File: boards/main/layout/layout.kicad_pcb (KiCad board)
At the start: 4 copper layers, 100 x 80 mm, 113 parts, among them J1 PPPC201LFBN-RC, J10 61300811121, J11 61300811121, J12 SJ1-3523N, J13 61300311121, J14 61300311121, J15 61300811121, J16 61300811121, J17 61300811121, J18 61300811121, J19 USB4085-GF-A, J2 PPPC201LFBN-RC, J3 61301021121, J4 connector, J5 61300211121, J6 61300211121, J7 SJ1-3523N, J8 61300811121, J9 61300811121, U1 ES8388, U10 NE5532DR, U2 ES8388, U3 LP2985-33DBVR, U4 MCP73831-2-OTI/OT, U5 HT8988A, U6 AP2114H-3.3TRG1, U7 CD4052BM96, U8 CD4052BM96, U9 NE5532DR

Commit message: layout
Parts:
- added C54: GRM188Z71A106KA73D, C_0603_1608Metric, F.Cu at (84.0, 30.0)
- added C55: GCM155R71H104KE02D, C_0402_1005Metric, F.Cu at (80.0, 46.0)
- added C56: GRM188Z71A106KA73D, C_0603_1608Metric, F.Cu at (84.0, 42.0)
- added C57: GCM155R71H104KE02D, C_0402_1005Metric, F.Cu at (86.0, 54.0)
- added C58: GRM188Z71A106KA73D, C_0603_1608Metric, F.Cu at (90.0, 80.0)
- added C59: GCM155R71H104KE02D, C_0402_1005Metric, F.Cu at (88.0, 70.0)
- added C60: GRM188Z71A106KA73D, C_0603_1608Metric, F.Cu at (82.0, 60.0)
- added C61: GCM155R71H104KE02D, C_0402_1005Metric, F.Cu at (94.0, 70.0)
- added R25: ERJ-2RKF1002X, R_0402_1005Metric, F.Cu at (75.4, 14.0)
- added R26: ERJ-2RKF1003X, R_0402_1005Metric, F.Cu at (68.5, 53.5)
- added R27: ERJ-2RKF1003X, R_0402_1005Metric, F.Cu at (81.0, 40.0)
- added U11: NE5532DR, SOIC-8_3.9x4.9mm_P1.27mm, F.Cu at (90.0, 64.4)
- C10: value GRM21BZ71A226ME15K -> GCM155R71H104KE02D; footprint C_0805_2012Metric -> C_0402_1005Metric
- C11: value GRM21BZ71E106KE15K -> GRM1555CYA103GE01D; footprint C_0805_2012Metric -> C_0402_1005Metric
- C14: value GRM21BZ71E106KE15K -> GRM21BZ71A226ME15K
- C15, C18: value GCM188R71E105KA64D -> GRM21BZ71E106KE15K; footprint C_0603_1608Metric -> C_0805_2012Metric
- C16, C17, C19, C20, C5: value capacitor -> GRM21BZ71E106KE15K
- C21, C22, C6: value GCM155R71H104KE02D -> GRM21BZ71E106KE15K; footprint C_0402_1005Metric -> C_0805_2012Metric
- C24, C26, C29: value GCM155R71H104KE02D -> capacitor; footprint C_0402_1005Metric -> C_0805_2012Metric
- C25, C9: value GRM21BZ71E106KE15K -> capacitor
- C27: value GRM21BZ71E106KE15K -> GCM155R71H104KE02D; footprint C_0805_2012Metric -> C_0402_1005Metric
- C28, C30: value GRM188Z71A106KA73D -> GCM155R71H104KE02D; footprint C_0603_1608Metric -> C_0402_1005Metric
- C7: value GRM1555CYA103GE01D -> GRM21BZ71E106KE15K; footprint C_0402_1005Metric -> C_0805_2012Metric
- R10, R9: value ERJ-2RKF1001X -> ERJ-2RKF1201X
- R11: value ERJ-2RKF4701X -> ERJ-2RKF1001X
- R14: value ERJ-2RKF1002X -> ERJ-2RKF4701X
- R15, R16: value ERJ-2RKF1002X -> ERJ-2RKF1001X
- R23, R24: value ERJ-2RKF1003X -> ERJ-2RKF1002X
- R3: value ERJ-2RKF1002X -> ERJ-3EKF4701V; footprint R_0402_1005Metric -> R_0603_1608Metric
- R4: value ERJ-2RKF5101X -> ERJ-3EKF4701V; footprint R_0402_1005Metric -> R_0603_1608Metric
- R5: value ERJ-2RKF5101X -> ERJ-2RKF1002X
- R6: value ERJ-2RKF1201X -> ERJ-2RKF1002X
- R7: value ERJ-2RKF1201X -> ERJ-2RKF5101X
- R8: value ERJ-2RKF1001X -> ERJ-2RKF5101X
- U3: value LP2985-33DBVR -> ES8388; footprint SOT-23-5 -> QFN-28-1EP_4x4mm_P0.4mm_EP2.4x2.4mm
- U4: value MCP73831-2-OTI/OT -> ES8388; footprint SOT-23-5 -> QFN-28-1EP_4x4mm_P0.4mm_EP2.4x2.4mm
- U5: value HT8988A -> LP2985-33DBVR; footprint QFN-28-1EP_4x4mm_P0.4mm_EP2.4x2.4mm -> SOT-23-5
- U6: value AP2114H-3.3TRG1 -> MCP73831-2-OTI/OT; footprint SOT-223-3_TabPin2 -> SOT-23-5
- U7: value CD4052BM96 -> AP2114H-3.3TRG1; footprint SOIC-16_3.9x9.9mm_P1.27mm -> SOT-223-3_TabPin2
- U9: value NE5532DR -> CD4052BM96; footprint SOIC-8_3.9x4.9mm_P1.27mm -> SOIC-16_3.9x9.9mm_P1.27mm
- moved R18 62.8 mm to (98.0, 26.0)
- moved R7 59.6 mm to (34.0, 45.5)
- moved R4 56.3 mm to (80.0, 78.0)
- moved U4 52.7 mm to (90.7, 47.9)
- moved C3 52.0 mm to (82.0, 80.0)
- moved C41 50.8 mm to (96.0, 26.0)
- moved C7 49.9 mm to (90.0, 82.0)
- moved U3 49.7 mm to (90.4, 42.0)
- moved R14 48.5 mm to (48.5, 47.5)
- moved C49 45.7 mm to (44.0, 47.5)
- moved C6 44.5 mm to (84.0, 28.0)
- moved C36 44.3 mm to (86.0, 58.0)
- moved R5 44.1 mm to (82.0, 38.0)
- moved C37 44.0 mm to (90.0, 70.0)
- moved U7 43.3 mm to (58.0, 53.0)
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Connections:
- net NC_DSDIN_A renamed NC_DSDIN_1
- net NC_DSDIN_B renamed NC_DSDIN_2
- net NC_LOUT1_A renamed NC_LOUT1_1
- net NC_LOUT1_B renamed NC_LOUT1_2
- net NC_LOUT2_A renamed NC_LOUT2_1
- net NC_LOUT2_B renamed NC_LOUT2_2
- net NC_MONO_A renamed NC_MONO_1
- net NC_MONO_B renamed NC_MONO_2
- net NC_ROUT1_A renamed NC_ROUT1_1
- net NC_ROUT1_B renamed NC_ROUT1_2
- net NC_ROUT2_A renamed NC_ROUT2_1
- net NC_ROUT2_B renamed NC_ROUT2_2
- C10 pad 1: DVDD -> VBAT
- C11 pad 1: DVREF_A1 -> LP2985_BYP
- C12 pad 1: DVREF_A2 -> DAC_OUTL
- C12 pad 2: AGND -> DAC_L_AC
- C13 pad 1: DVRP_A1 -> DAC_OUTR
- C13 pad 2: AGND -> DAC_R_AC
- C14 pad 1: DVRP_A2 -> DVDD
- C14 pad 2: AGND -> DGND
- C15 pad 1: HPCOM -> DVREF_A1
- C16 pad 1: HP_OUTL -> DVREF_A2
- C16 pad 2: HP_AC_L -> AGND
- C17 pad 1: HP_OUTR -> DVREF_A3
- C17 pad 2: HP_AC_R -> AGND
- C18 pad 1: LCOM -> DVREF_A4
- C19 pad 1: MUX1_X_FILT -> DVRP_A1
- C19 pad 2: OUT_L_AC -> AGND
- C20 pad 1: MUX1_Y_FILT -> DVRP_A2
- C20 pad 2: OUT_R_AC -> AGND
- C21 pad 1: MUX1_X_FILT -> DVRP_A3
- C22 pad 1: MUX1_Y_FILT -> DVRP_A4
- C23 pad 1: VBUS -> HP_OUTL
- C23 pad 2: DGND -> HP_AC_L
- C24 pad 1: VBUS -> HP_OUTR
- C24 pad 2: DGND -> HP_AC_R
- C25 pad 1: VMID -> MUX1_X_FILT
- C25 pad 2: AGND -> OUT_L_AC
- C26 pad 1: VBAT_DIV -> MUX1_Y_FILT
- C26 pad 2: DGND -> OUT_R_AC
- C27 pad 1: VREF -> MUX1_X_FILT
- C28 pad 1: AVDD -> MUX1_Y_FILT
- C29 pad 1: AVDD -> VBUS
- C29 pad 2: AGND -> DGND
- C3 pad 1: VRP_A1 -> VREF_A3
- C30 pad 1: AVDD -> VBUS
- C30 pad 2: AGND -> DGND
- C31 pad 1: AVDD -> VBAT_DIV
- C31 pad 2: AGND -> DGND
- C36 pad 1: DVDD -> AVDD
- C36 pad 2: DGND -> AGND
- C37 pad 1: DVDD -> AVDD
- C37 pad 2: DGND -> AGND
- C38 pad 1: DVDD -> AVDD
- C38 pad 2: DGND -> AGND
- C39 pad 1: DVDD -> AVDD
- C39 pad 2: DGND -> AGND
- C4 pad 1: VRP_A2 -> VREF_A4
- C40 pad 1: DVDD -> AVDD
- C40 pad 2: DGND -> AGND
- C41 pad 1: DVDD -> AVDD
- C41 pad 2: DGND -> AGND
- C46 pad 1: AVDD -> DVDD
- C46 pad 2: AGND -> DGND
- C47 pad 1: AVDD -> DVDD
- C47 pad 2: AGND -> DGND
- C48 pad 1: AVDD -> DVDD
- C48 pad 2: AGND -> DGND
- C49 pad 1: AVDD -> DVDD
- C49 pad 2: AGND -> DGND
- C5 pad 1: VBAT -> VRP_A1
- C5 pad 2: DGND -> AGND
- C50 pad 1: AVDD -> DVDD
- C50 pad 2: AGND -> DGND
- C51 pad 1: AVDD -> DVDD
- C51 pad 2: AGND -> DGND
- C52 pad 1: AVDD -> DVDD
- C52 pad 2: AGND -> DGND
- C53 pad 1: AVDD -> DVDD
- C53 pad 2: AGND -> DGND
- C6 pad 1: VBAT -> VRP_A2
- C6 pad 2: DGND -> AGND
- C7 pad 1: LP2985_BYP -> VRP_A3
- C8 pad 1: DAC_OUTL -> VRP_A4
- C8 pad 2: DAC_L_AC -> AGND
- C9 pad 1: DAC_OUTR -> VBAT
- C9 pad 2: DAC_R_AC -> DGND
- J1 pad 4: NC_GPIO4 -> ADCDAT_C
- J2 pad 16: NC_GPIO48 -> ADCDAT_D
- J2 pad 2: NC_GPIO43 -> SDA2
- J2 pad 20: DOUT_DAC -> DACDAT
- J2 pad 3: NC_GPIO44 -> SCL2
- R10 pad 1: OUT_R_AC -> SUM_FB_R
- R10 pad 2: JACK_R_TIP -> SUM_R
- R11 pad 1: PROG_PIN -> VBUS
- R11 pad 2: DGND -> LED_STAT
- R12 pad 1: MUX1_X_OUT -> OUT_L_AC
- R12 pad 2: MUX1_X_FILT -> JACK_L_TIP
- R13 pad 1: MUX1_Y_OUT -> OUT_R_AC
- R13 pad 2: MUX1_Y_FILT -> JACK_R_TIP
- R14 pad 1: SIG_CH1 -> PROG_PIN
- R14 pad 2: SUM_FB_L -> DGND
- R15 pad 1: SIG_CH2 -> MUX1_X_OUT
- R15 pad 2: SUM_FB_L -> MUX1_X_FILT
- R16 pad 1: SIG_CH3 -> MUX1_Y_OUT
- R16 pad 2: SUM_FB_L -> MUX1_Y_FILT
- R17 pad 1: SIG_CH4 -> SIG_CH1
- R18 pad 1: SIG_CH5 -> SIG_CH2
- R18 pad 2: SUM_FB_R -> SUM_FB_L
- R19 pad 1: SIG_CH6 -> SIG_CH3
- R19 pad 2: SUM_FB_R -> SUM_FB_L
- R20 pad 1: SIG_CH7 -> SIG_CH4
- R20 pad 2: SUM_FB_R -> SUM_FB_L
- R21 pad 1: SIG_CH8 -> SIG_CH5
- R22 pad 1: DVDD -> SIG_CH6
- R22 pad 2: UART_SLAVE_TX -> SUM_FB_R
- R23 pad 1: VBAT_DIV -> SIG_CH7
- R23 pad 2: DGND -> SUM_FB_R
- R24 pad 1: VBAT -> SIG_CH8
- R24 pad 2: VBAT_DIV -> SUM_FB_R
- R3 pad 2: AD0_HIGH -> SCL2
- R4 pad 1: CC1 -> AVDD
- R4 pad 2: DGND -> SDA2
- R5 pad 1: CC2 -> AVDD
- R5 pad 2: DGND -> AD0_HIGH
- R6 pad 1: SUM_FB_L -> AVDD
- R6 pad 2: SUM_L -> AD0_HIGH_2
- R7 pad 1: SUM_FB_R -> CC1
- R7 pad 2: SUM_R -> DGND
- R8 pad 1: VBUS -> CC2
- R8 pad 2: LED_STAT -> DGND
- R9 pad 1: OUT_L_AC -> SUM_FB_L
- R9 pad 2: JACK_L_TIP -> SUM_L
- U1 pad 16: SIG_CH3 -> NC_LIN2_1
- U1 pad 17: SIG_CH4 -> NC_RIN2_1
- U10 pad 1: SUM_L -> OUT_L
- U10 pad 2: SUM_FB_L -> OUT_L
- U10 pad 3: AGND -> SUM_L
- U10 pad 5: AGND -> SUM_R
- U10 pad 6: SUM_FB_R -> OUT_R
- U10 pad 7: SUM_R -> OUT_R
- U2 pad 16: SIG_CH7 -> NC_LIN2_2
- U2 pad 17: SIG_CH8 -> NC_RIN2_2
- U2 pad 18: SIG_CH5 -> SIG_CH3
- U2 pad 19: SIG_CH6 -> SIG_CH4
- U3 pad 1: VBAT -> DVDD
- U3 pad 2: AGND -> HP_OUTL
- U3 pad 3: VBAT -> HP_OUTR
- U3 pad 4: LP2985_BYP -> AVDD
- U3 pad 5: AVDD -> AGND
- U4 pad 1: CHARGE_STAT -> DVDD
- U4 pad 2: DGND -> NC_LOUT1_4
- U4 pad 3: VBAT_RAW -> NC_ROUT1_4
- U4 pad 4: VBUS -> AVDD
- U4 pad 5: PROG_PIN -> AGND
- U5 pad 1: DVDD -> VBAT
- U5 pad 2: DVDD -> AGND
- U5 pad 3: DVDD -> VBAT
- U5 pad 4: DGND -> LP2985_BYP
- U5 pad 5: DGND -> AVDD
- U6 pad 1: DGND -> CHARGE_STAT
- U6 pad 2: DVDD -> DGND
- U6 pad 3: VBAT -> VBAT_RAW
- U7 pad 1: DAC_R_AC -> DGND
- U7 pad 2: OUT_R -> DVDD
- U7 pad 3: MUX1_Y_OUT -> VBAT
- U8 pad 1: NC_MUX2_Y1 -> DAC_R_AC
- U8 pad 11: NC_MUX2_X3 -> OUT_L
- U8 pad 12: MUX2_X_OUT -> MUX1_X_OUT
- U8 pad 13: NC_MUX2_X0 -> OUT_L
- U8 pad 14: NC_MUX2_X1 -> DAC_L_AC
- U8 pad 15: DAC_L_AC -> OUT_L
- U8 pad 2: NC_MUX2_Y0 -> OUT_R
- U8 pad 3: MUX2_Y_OUT -> MUX1_Y_OUT
- U8 pad 4: DAC_R_AC -> OUT_R
- U8 pad 5: NC_MUX2_Y3 -> DAC_R_AC
- U9 pad 1: OUT_L -> NC_MUX2_Y1
- U9 pad 2: OUT_L -> NC_MUX2_Y0
- U9 pad 3: SUM_L -> MUX2_Y_OUT
- U9 pad 4: AGND -> DAC_R_AC
- U9 pad 5: SUM_R -> NC_MUX2_Y3
- U9 pad 6: OUT_R -> MUX_INH
- U9 pad 7: OUT_R -> AGND
- U9 pad 8: AVDD -> AGND
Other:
- board text added: "ADC CH1+2"
- board text added: "ADC CH3+4"
- board text added: "ADC CH5+6 / DAC"
- board text added: "ADC CH7+8"
- board text removed: "ADC CH1-4"
- board text removed: "ADC CH5-8"
- board text removed: "DAC"

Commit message: yout
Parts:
- J13, J14: value 61300311121 -> 61300211121; footprint PinHeader_1x03_P2.54mm_Vertical -> PinHeader_1x02_P2.54mm_Vertical
- moved C31 66.7 mm to (20.0, 59.7)
- moved C7 66.6 mm to (81.0, 16.0)
- moved R18 64.3 mm to (81.0, 88.0)
- moved R27 61.1 mm to (24.5, 63.2)
- moved R17 58.0 mm to (85.0, 84.0)
- moved R1 57.5 mm to (24.5, 59.7)
- moved R25 56.0 mm to (75.4, 70.0)
- moved C24 54.1 mm to (101.0, 28.0)
- moved C23 50.9 mm to (97.0, 28.0)
- moved R21 50.5 mm to (87.0, 84.0)
- moved R26 49.5 mm to (20.0, 63.2)
- moved R3 48.8 mm to (93.0, 30.0)
- moved C46 41.0 mm to (93.0, 34.0)
- moved C52 38.3 mm to (93.0, 38.0)
- moved R23 38.0 mm to (81.0, 84.0)
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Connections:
- net JACK_L_TIP renamed JACK_A_TIP
- net JACK_R_TIP renamed JACK_B_TIP
- net OUT_L renamed OUT_A
- net OUT_L_AC renamed OUT_A_AC
- net OUT_R renamed OUT_B
- net OUT_R_AC renamed OUT_B_AC
- net SUM_FB_L renamed SUM_FB_A
- net SUM_FB_R renamed SUM_FB_B
- net SUM_L renamed SUM_A
- net SUM_R renamed SUM_B
- C31 pad 1: VBAT_DIV -> VBAT_MON
- J13 pad 2: JACK_L_RING -> AGND
- J14 pad 2: JACK_R_RING -> AGND
- J3 pad 9: AVDD -> VBAT
- R26 pad 1: VBAT_DIV -> VBAT_MON
- R27 pad 2: VBAT_DIV -> VBAT_MON
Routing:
- added copper zone on B.Cu, net AGND
- added copper zone on F.Cu, net AGND
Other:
- board text removed: "MAIN OUT L"
- board text removed: "MAIN OUT R"

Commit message: ground plane moat etc
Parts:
- moved R1 75.5 mm to (93.0, 28.0)
- moved R25 56.0 mm to (75.4, 14.0)
- moved C13 34.5 mm to (99.0, 84.0)
- moved C7 32.3 mm to (93.0, 46.0)
- moved R3 32.3 mm to (81.0, 60.0)
- moved C3 30.5 mm to (93.0, 38.0)
- moved C23 23.4 mm to (89.0, 50.0)
- moved R23 22.8 mm to (87.0, 62.0)
- moved R19 22.4 mm to (83.0, 84.0)
- moved C12 22.0 mm to (107.0, 80.0)
- moved C8 21.5 mm to (81.0, 62.0)
- moved C25 20.1 mm to (107.0, 58.0)
- moved C6 19.7 mm to (101.0, 28.0)
- moved R4 18.4 mm to (95.0, 48.0)
- moved C17 17.9 mm to (89.0, 42.0)
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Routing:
- net MCLK: track 0.00 -> 46.9 mm, vias 0 -> 4
- net BCLK: track 0.00 -> 41.0 mm, vias 0 -> 4
- net LRCK: track 0.00 -> 36.4 mm, vias 0 -> 4
- net SCL2: track 0.00 -> 18.3 mm, vias 0 -> 2
- net SCL: track 0.00 -> 18.2 mm, vias 0 -> 2
- net SDA2: track 0.00 -> 18.2 mm, vias 0 -> 2
- net SDA: track 0.00 -> 18.1 mm, vias 0 -> 2
- net ADCDAT_D: track 0.00 -> 9.10 mm, vias 0 -> 1
- net DACDAT: track 0.00 -> 9.09 mm, vias 0 -> 1
- net ADCDAT_B: track 0.00 -> 9.08 mm, vias 0 -> 1
- net ADCDAT_A: track 0.00 -> 9.08 mm, vias 0 -> 1
- net ADCDAT_C: track 0.00 -> 9.06 mm, vias 0 -> 1
- added copper zone on In1.Cu, net DGND

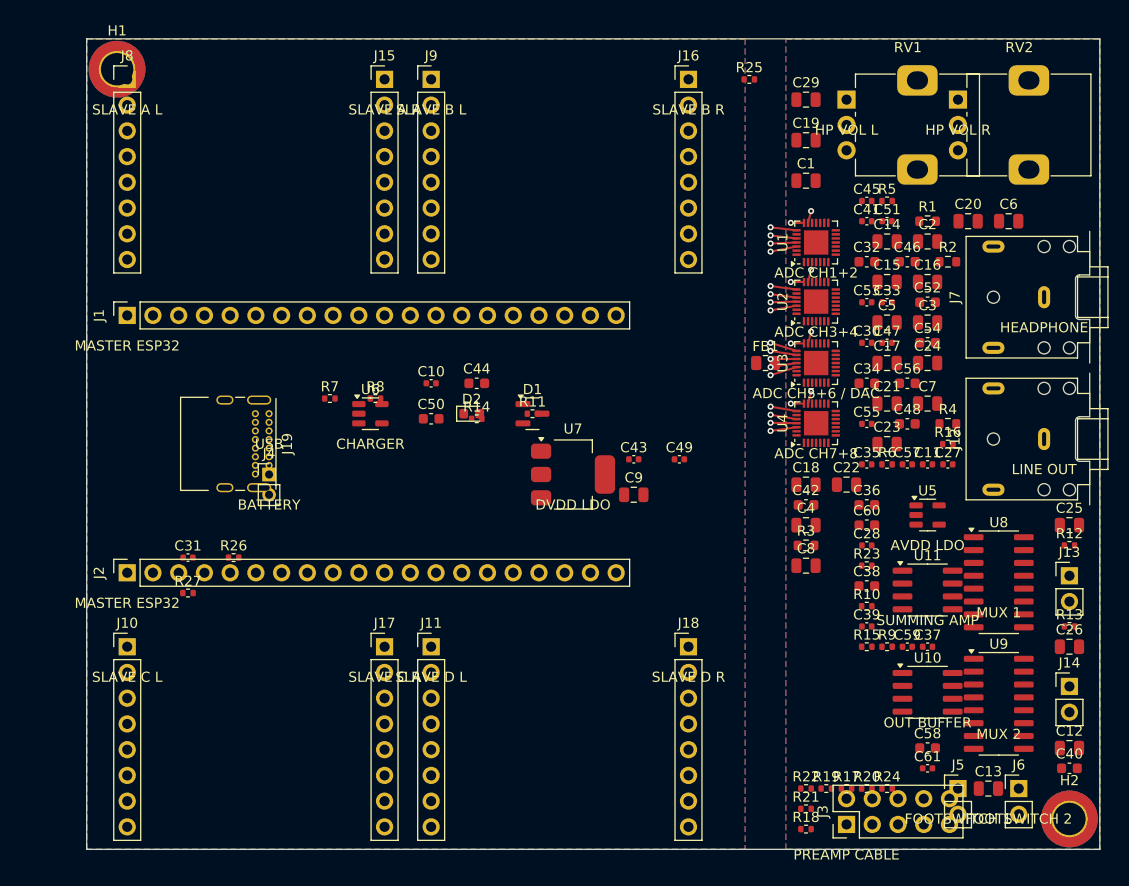
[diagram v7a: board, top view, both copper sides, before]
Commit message: esp32 footprint, layout changes, removed charging usb
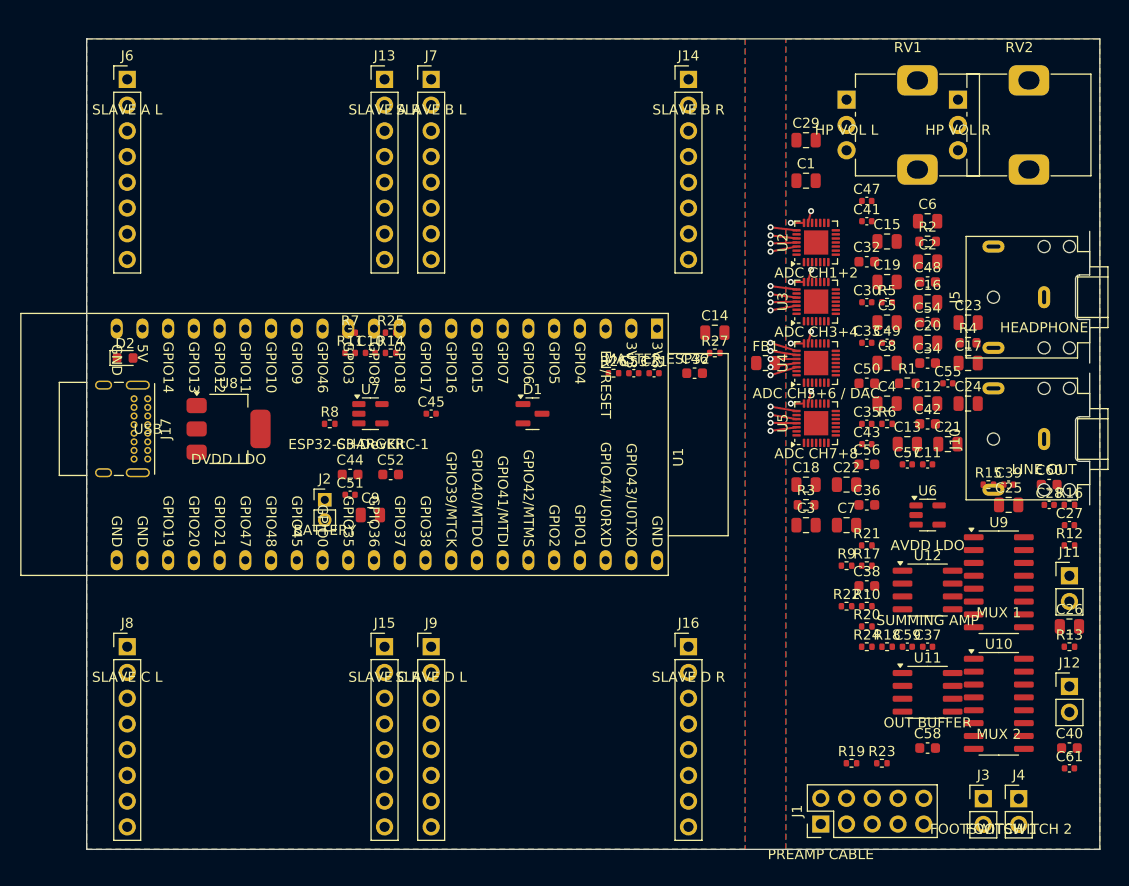
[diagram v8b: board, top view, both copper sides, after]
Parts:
- removed H1, H2: ?, MountingHole_3.2mm_M3_DIN965_Pad_TopBottom
- removed J18: 61300811121, PinHeader_1x08_P2.54mm_Vertical
- removed J19: USB4085-GF-A, USB_C_Receptacle_GCT_USB4085
- added U12: NE5532DR, SOIC-8_3.9x4.9mm_P1.27mm, F.Cu at (93.0, 64.4)
- J1: value PPPC201LFBN-RC -> 61301021121; footprint PinSocket_1x20_P2.54mm_Vertical -> PinHeader_2x05_P2.54mm_Vertical
- J10: value 61300811121 -> SJ1-3523N; footprint PinHeader_1x08_P2.54mm_Vertical -> Jack_3.5mm_CUI_SJ1-3523N_Horizontal
- J11: value 61300811121 -> 61300211121; footprint PinHeader_1x08_P2.54mm_Vertical -> PinHeader_1x02_P2.54mm_Vertical
- J12: value SJ1-3523N -> 61300211121; footprint Jack_3.5mm_CUI_SJ1-3523N_Horizontal -> PinHeader_1x02_P2.54mm_Vertical
- J13, J14, J6: value 61300211121 -> 61300811121; footprint PinHeader_1x02_P2.54mm_Vertical -> PinHeader_1x08_P2.54mm_Vertical
- J17: value 61300811121 -> USB4085-GF-A; footprint PinHeader_1x08_P2.54mm_Vertical -> USB_C_Receptacle_GCT_USB4085
- J2: value PPPC201LFBN-RC -> connector; footprint PinSocket_1x20_P2.54mm_Vertical -> PinHeader_1x02_P2.00mm_Vertical
- J3: value 61301021121 -> 61300211121; footprint PinHeader_2x05_P2.54mm_Vertical -> PinHeader_1x02_P2.54mm_Vertical
- J4: value connector -> 61300211121; footprint PinHeader_1x02_P2.00mm_Vertical -> PinHeader_1x02_P2.54mm_Vertical
- J5: value 61300211121 -> SJ1-3523N; footprint PinHeader_1x02_P2.54mm_Vertical -> Jack_3.5mm_CUI_SJ1-3523N_Horizontal
- J7: value SJ1-3523N -> 61300811121; footprint Jack_3.5mm_CUI_SJ1-3523N_Horizontal -> PinHeader_1x08_P2.54mm_Vertical
- U1: value ES8388 -> ESP32-S3-DevKitC-1; footprint QFN-28-1EP_4x4mm_P0.4mm_EP2.4x2.4mm -> ESP32-S3-DevKitC
- U10: value NE5532DR -> CD4052BM96; footprint SOIC-8_3.9x4.9mm_P1.27mm -> SOIC-16_3.9x9.9mm_P1.27mm
- U5: value LP2985-33DBVR -> ES8388; footprint SOT-23-5 -> QFN-28-1EP_4x4mm_P0.4mm_EP2.4x2.4mm
- U6: value MCP73831-2-OTI/OT -> LP2985-33DBVR
- U7: value AP2114H-3.3TRG1 -> MCP73831-2-OTI/OT; footprint SOT-223-3_TabPin2 -> SOT-23-5
- U8: value CD4052BM96 -> AP2114H-3.3TRG1; footprint SOIC-16_3.9x9.9mm_P1.27mm -> SOT-223-3_TabPin2
- moved J6 112.4 mm to (14.0, 14.0)
- moved J10 92.8 mm to (104.5, 49.5), turned to 90 degrees
- moved J1 84.9 mm to (82.5, 87.5)
- moved J13 83.5 mm to (39.4, 14.0)
- moved J4 80.6 mm to (102.0, 85.0)
- moved U8 77.5 mm to (24.0, 48.5)
- moved J14 70.7 mm to (69.4, 14.0)
- moved J7 64.2 mm to (44.0, 14.0), turned to 0 degrees
- moved J11 63.4 mm to (107.0, 63.0)
- moved C51 59.5 mm to (36.0, 55.0)
- moved R27 57.1 mm to (72.0, 41.0)
- moved J15 56.0 mm to (39.4, 70.0)
- moved J16 56.0 mm to (69.4, 70.0)
- moved J8 56.0 mm to (14.0, 70.0)
- moved J9 56.0 mm to (44.0, 70.0)
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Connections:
- J1 pad 1: DVDD -> SIG_CH1
- J1 pad 10: SD_FWD_AB -> AGND
- J1 pad 2: DVDD -> SIG_CH2
- J1 pad 3: ESP_RST -> SIG_CH3
- J1 pad 4: ADCDAT_C -> SIG_CH4
- J1 pad 5: MCLK -> SIG_CH5
- J1 pad 6: BCLK -> SIG_CH6
- J1 pad 7: LRCK -> SIG_CH7
- J1 pad 8: ADCDAT_A -> SIG_CH8
- J1 pad 9: ADCDAT_B -> VBAT
- J11 pad 1: DVDD -> JACK_A_TIP
- J11 pad 2: DVDD -> AGND
- J13 pad 1: JACK_A_TIP -> DGND
- J13 pad 2: AGND -> NC_SA_GPIO43
- J14 pad 1: JACK_B_TIP -> DGND
- J14 pad 2: AGND -> NC_SB_GPIO43
- J15 pad 2: NC_SA_GPIO43 -> NC_SC_GPIO43
- J15 pad 3: NC_SA_GPIO44 -> NC_SC_GPIO44
- J15 pad 4: NC_SA_GPIO1 -> NC_SC_GPIO1
- J15 pad 5: NC_SA_GPIO2 -> NC_SC_GPIO2
- J15 pad 6: NC_SA_GPIO42 -> NC_SC_GPIO42
- J15 pad 8: SD_FWD_AB -> SD_FWD_CD
- J16 pad 2: NC_SB_GPIO43 -> NC_SD_GPIO43
- J16 pad 3: NC_SB_GPIO44 -> NC_SD_GPIO44
- J16 pad 4: NC_SB_GPIO1 -> NC_SD_GPIO1
- J16 pad 5: NC_SB_GPIO2 -> NC_SD_GPIO2
- J16 pad 6: NC_SB_GPIO42 -> NC_SD_GPIO42
- J16 pad 8: SD_FWD_AB -> SD_FWD_CD
- J2 pad 1: DGND -> VBAT_RAW
- J2 pad 2: SDA2 -> DGND
- J3 pad 1: SIG_CH1 -> FS1_A
- J3 pad 2: SIG_CH2 -> FS1_B
- J4 pad 1: VBAT_RAW -> FS2_A
- J4 pad 2: DGND -> FS2_B
- J6 pad 1: FS2_A -> DVDD
- J6 pad 2: FS2_B -> DVDD
- J8 pad 3: EN_SLAVE2 -> EN_SLAVE4
- J8 pad 4: NC_SA_GPIO4 -> NC_SC_GPIO4
- J8 pad 7: DIN_A -> DIN_C
- J8 pad 8: NC_SA_GPIO15 -> NC_SC_GPIO15
- J9 pad 3: EN_SLAVE3 -> EN_SLAVE5
- J9 pad 4: NC_SB_GPIO4 -> NC_SD_GPIO4
- J9 pad 7: DIN_B -> DIN_D
- J9 pad 8: NC_SB_GPIO15 -> NC_SD_GPIO15
- U1 pad 10: DVREF_A1 -> SD_FWD_AB
- U1 pad 11: DVRP_A1 -> SD_FWD_CD
- U1 pad 12: NC_MONO_1 -> BCLK_OUT
- U1 pad 13: VRP_A1 -> NC_GPIO3
- U1 pad 14: VREF_A1 -> MUX_B
- U1 pad 15: AVDD -> LRCK_OUT
- U1 pad 16: NC_LIN2_1 -> DIN_A
- U1 pad 17: NC_RIN2_1 -> DIN_B
- U1 pad 18: SIG_CH1 -> DIN_C
- U1 pad 19: SIG_CH2 -> DACDAT
- U1 pad 2: NC_LOUT1_1 -> DVDD
- U1 pad 20: MCLK -> DIN_D
- U1 pad 21: BCLK -> NC_5V
- U1 pad 22: LRCK -> DGND
- U1 pad 23: NC_DSDIN_1 -> DGND
- U1 pad 24: ADCDAT_A -> DGND
- U1 pad 25: SDA -> USB_DN
- U1 pad 26: SCL -> USB_DP
- U1 pad 27: AGND -> SDA
- U1 pad 28: DVDD -> BOOT_SLAVE5
- U1 pad 29: AGND -> ADCDAT_D
- U1 pad 3: NC_ROUT1_1 -> ESP_RST
- U1 pad 4: AVDD -> ADCDAT_C
- U1 pad 5: AGND -> MCLK
- U1 pad 6: NC_ROUT2_1 -> BCLK
- U1 pad 7: NC_LOUT2_1 -> LRCK
- U1 pad 8: DVDD -> ADCDAT_A
- U1 pad 9: DGND -> ADCDAT_B
- U10 pad 1: OUT_A -> NC_MUX2_Y1
- U10 pad 2: OUT_A -> NC_MUX2_Y0
- U10 pad 3: SUM_A -> MUX2_Y_OUT
- U10 pad 4: AGND -> DAC_R_AC
- U10 pad 5: SUM_B -> NC_MUX2_Y3
- U10 pad 6: OUT_B -> MUX_INH
- U10 pad 7: OUT_B -> AGND
- U10 pad 8: AVDD -> AGND
- U11 pad 1: SUM_A -> OUT_A
- U11 pad 2: SUM_FB_A -> OUT_A
- U11 pad 3: AGND -> SUM_A
- U11 pad 5: AGND -> SUM_B
- U11 pad 6: SUM_FB_B -> OUT_B
- U11 pad 7: SUM_B -> OUT_B
- U2 pad 10: DVREF_A2 -> DVREF_A1
- U2 pad 11: DVRP_A2 -> DVRP_A1
- U2 pad 12: NC_MONO_2 -> NC_MONO_1
- U2 pad 13: VRP_A2 -> VRP_A1
- U2 pad 14: VREF_A2 -> VREF_A1
- U2 pad 16: NC_LIN2_2 -> NC_LIN2_1
- U2 pad 17: NC_RIN2_2 -> NC_RIN2_1
- U2 pad 18: SIG_CH3 -> SIG_CH1
- U2 pad 19: SIG_CH4 -> SIG_CH2
- U2 pad 2: NC_LOUT1_2 -> NC_LOUT1_1
- U2 pad 23: NC_DSDIN_2 -> NC_DSDIN_1
- U2 pad 24: ADCDAT_B -> ADCDAT_A
- U2 pad 27: AD0_HIGH -> AGND
- U2 pad 3: NC_ROUT1_2 -> NC_ROUT1_1
- U2 pad 6: NC_ROUT2_2 -> NC_ROUT2_1
- U2 pad 7: NC_LOUT2_2 -> NC_LOUT2_1
- U3 pad 10: DVREF_A3 -> DVREF_A2
- U3 pad 11: DVRP_A3 -> DVRP_A2
- U3 pad 12: NC_MONO_3 -> NC_MONO_2
- U3 pad 13: VRP_A3 -> VRP_A2
- U3 pad 14: VREF_A3 -> VREF_A2
- U3 pad 16: NC_LIN2_3 -> NC_LIN2_2
- U3 pad 17: NC_RIN2_3 -> NC_RIN2_2
- U3 pad 18: SIG_CH5 -> SIG_CH3
- U3 pad 19: SIG_CH6 -> SIG_CH4
- U3 pad 2: HP_OUTL -> NC_LOUT1_2
- U3 pad 23: DACDAT -> NC_DSDIN_2
- U3 pad 24: ADCDAT_C -> ADCDAT_B
- U3 pad 25: SDA2 -> SDA
- U3 pad 26: SCL2 -> SCL
- U3 pad 27: AGND -> AD0_HIGH
- U3 pad 3: HP_OUTR -> NC_ROUT1_2
- U3 pad 6: DAC_OUTR -> NC_ROUT2_2
- U3 pad 7: DAC_OUTL -> NC_LOUT2_2
- U4 pad 10: DVREF_A4 -> DVREF_A3
- U4 pad 11: DVRP_A4 -> DVRP_A3
- U4 pad 12: NC_MONO_4 -> NC_MONO_3
- U4 pad 13: VRP_A4 -> VRP_A3
- U4 pad 14: VREF_A4 -> VREF_A3
- U4 pad 16: NC_LIN2_4 -> NC_LIN2_3
- U4 pad 17: NC_RIN2_4 -> NC_RIN2_3
- U4 pad 18: SIG_CH7 -> SIG_CH5
- U4 pad 19: SIG_CH8 -> SIG_CH6
- U4 pad 2: NC_LOUT1_4 -> HP_OUTL
- U4 pad 23: NC_DSDIN_4 -> DACDAT
- U4 pad 24: ADCDAT_D -> ADCDAT_C
- U4 pad 27: AD0_HIGH_2 -> AGND
- U4 pad 3: NC_ROUT1_4 -> HP_OUTR
- U4 pad 6: NC_ROUT2_4 -> DAC_OUTR
- U4 pad 7: NC_LOUT2_4 -> DAC_OUTL
- U5 pad 1: VBAT -> DVDD
- U5 pad 2: AGND -> NC_LOUT1_4
- U5 pad 3: VBAT -> NC_ROUT1_4
- U5 pad 4: LP2985_BYP -> AVDD
- U5 pad 5: AVDD -> AGND
- U6 pad 1: CHARGE_STAT -> VBAT
- U6 pad 2: DGND -> AGND
- U6 pad 3: VBAT_RAW -> VBAT
- U6 pad 4: VBUS -> LP2985_BYP
- U6 pad 5: PROG_PIN -> AVDD
- U7 pad 1: DGND -> CHARGE_STAT
- U7 pad 2: DVDD -> DGND
- U7 pad 3: VBAT -> VBAT_RAW
- U8 pad 1: DAC_R_AC -> DGND
- U8 pad 2: OUT_B -> DVDD
- U8 pad 3: MUX1_Y_OUT -> VBAT
- U9 pad 1: NC_MUX2_Y1 -> DAC_R_AC
- U9 pad 11: NC_MUX2_X3 -> OUT_A
- U9 pad 12: MUX2_X_OUT -> MUX1_X_OUT
- U9 pad 13: NC_MUX2_X0 -> OUT_A
- U9 pad 14: NC_MUX2_X1 -> DAC_L_AC
- U9 pad 15: DAC_L_AC -> OUT_A
- U9 pad 2: NC_MUX2_Y0 -> OUT_B
- U9 pad 3: MUX2_Y_OUT -> MUX1_Y_OUT
- U9 pad 4: DAC_R_AC -> OUT_B
- U9 pad 5: NC_MUX2_Y3 -> DAC_R_AC
